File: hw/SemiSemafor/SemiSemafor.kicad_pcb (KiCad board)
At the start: 2 copper layers, 40.2 x 63.1 mm, 44 parts, among them J1 USB_PCB, J2 ESP-Programing_conector, SW1 SW_DIP_x01, SW2 SW_DIP_x01, U1 LD39200, U2 ESP32-C3-MINI-1, U3 LIS2DH12

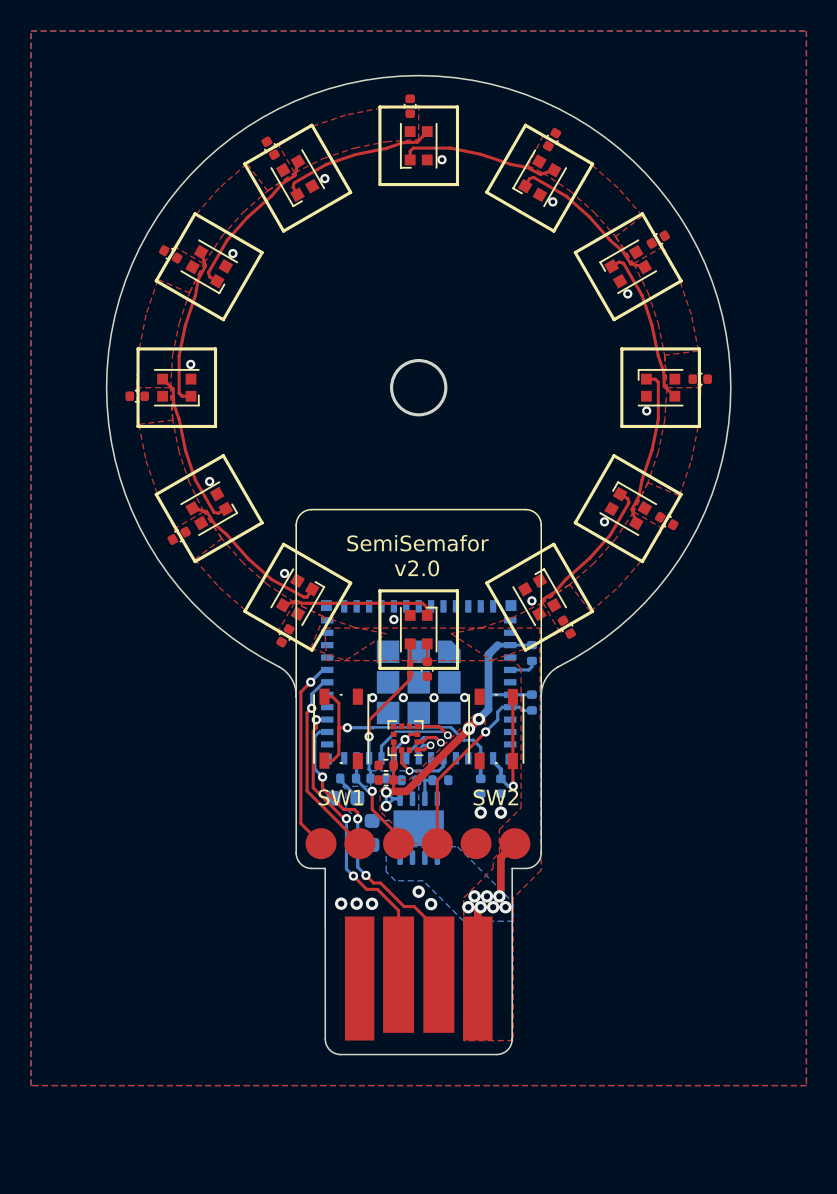
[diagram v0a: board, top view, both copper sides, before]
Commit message: 5mm LED
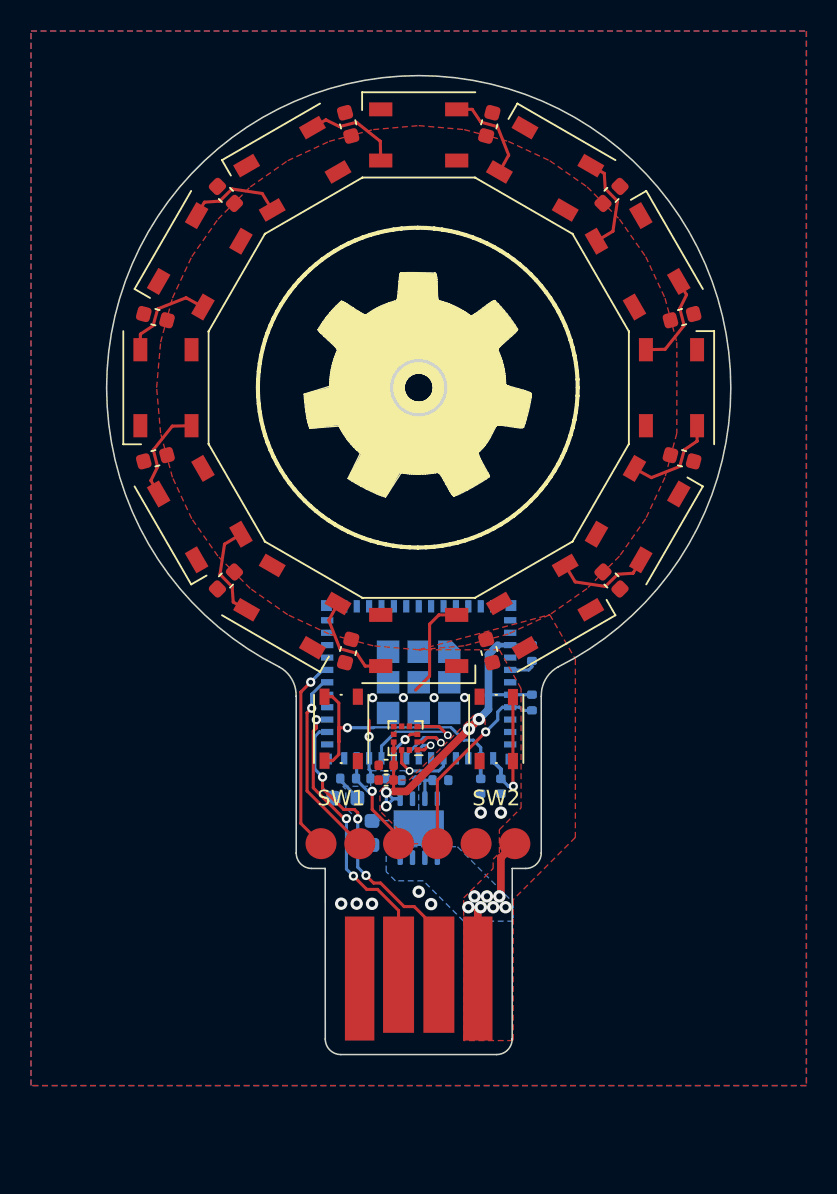
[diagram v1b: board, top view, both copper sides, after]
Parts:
- removed FB1: FerriteBead, Inductor_SMD:L_0201_0603Metric
- C1, C10, C11, C12, C13, C14, C15, C2, C3, C4, C5, C9: footprint Capacitor_SMD:C_0402_1005Metric -> Capacitor_SMD:C_0603_1608Metric
- D1, D10, D11, D12, D2, D3, D4, D5, D6, D7, D8, D9: footprint LED_SMD:LED_WS2812B-2020_PLCC4_2.0x2.0mm -> LED_SMD:LED_WS2812B_PLCC4_5.0x5.0mm_P3.2mm
- moved C11 5.23 mm to (162.4, 67.6), turned to 45 degrees
- moved C2 5.23 mm to (137.6, 92.4), turned to -135 degrees
- moved C14 5.23 mm to (162.4, 92.4), turned to -45 degrees
- moved C5 5.23 mm to (137.6, 67.6), turned to 135 degrees
- moved C12 5.23 mm to (167.0, 75.5), turned to 15 degrees
- moved C3 5.23 mm to (133.0, 84.5), turned to -165 degrees
- moved C9 5.23 mm to (145.5, 63.0), turned to 105 degrees
- moved C15 5.23 mm to (154.5, 97.0), turned to -75 degrees
- moved C1 5.23 mm to (145.4, 97.0), turned to -105 degrees
- moved C10 5.23 mm to (154.6, 63.0), turned to 75 degrees
- moved C13 5.23 mm to (167.0, 84.5), turned to -15 degrees
- moved C4 5.23 mm to (133.0, 75.5), turned to 165 degrees
- moved D11 0.70 mm to (164.1, 88.2), turned to 60 degrees
- moved D3 0.70 mm to (135.9, 88.2), turned to -60 degrees
- moved D5 0.70 mm to (135.9, 71.8), turned to -120 degrees
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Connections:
- D1 pad 1: Net-(D1-DOUT) -> +5V
- D1 pad 2: GND -> Net-(D1-DOUT)
- D1 pad 3: Net-(D1-DIN) -> GND
- D1 pad 4: +5V -> Net-(D1-DIN)
- D10 pad 1: Net-(D10-DOUT) -> +5V
- D10 pad 2: GND -> Net-(D10-DOUT)
- D10 pad 3: Net-(D10-DIN) -> GND
- D10 pad 4: +5V -> Net-(D10-DIN)
- D11 pad 1: Net-(D11-DOUT) -> +5V
- D11 pad 2: GND -> Net-(D11-DOUT)
- D11 pad 3: Net-(D10-DOUT) -> GND
- D11 pad 4: +5V -> Net-(D10-DOUT)
- D12 pad 1: unconnected-(D12-DOUT-Pad1) -> +5V
- D12 pad 2: GND -> (no net)
- D12 pad 3: Net-(D11-DOUT) -> GND
- D12 pad 4: +5V -> Net-(D11-DOUT)
- D2 pad 1: Net-(D2-DOUT) -> +5V
- D2 pad 2: GND -> Net-(D2-DOUT)
- D2 pad 3: Net-(D1-DOUT) -> GND
- D2 pad 4: +5V -> Net-(D1-DOUT)
- D3 pad 1: Net-(D3-DOUT) -> +5V
- D3 pad 2: GND -> Net-(D3-DOUT)
- D3 pad 3: Net-(D2-DOUT) -> GND
- D3 pad 4: +5V -> Net-(D2-DOUT)
- D4 pad 1: Net-(D4-DOUT) -> +5V
- D4 pad 2: GND -> Net-(D4-DOUT)
- D4 pad 3: Net-(D3-DOUT) -> GND
- D4 pad 4: +5V -> Net-(D3-DOUT)
- D5 pad 1: Net-(D5-DOUT) -> +5V
- D5 pad 2: GND -> Net-(D5-DOUT)
- D5 pad 3: Net-(D4-DOUT) -> GND
- D5 pad 4: +5V -> Net-(D4-DOUT)
- D6 pad 1: Net-(D6-DOUT) -> +5V
- D6 pad 2: GND -> Net-(D6-DOUT)
- D6 pad 3: Net-(D5-DOUT) -> GND
- D6 pad 4: +5V -> Net-(D5-DOUT)
- D7 pad 1: Net-(D7-DOUT) -> +5V
- D7 pad 2: GND -> Net-(D7-DOUT)
- D7 pad 3: Net-(D6-DOUT) -> GND
- D7 pad 4: +5V -> Net-(D6-DOUT)
- D8 pad 1: Net-(D8-DOUT) -> +5V
- D8 pad 2: GND -> Net-(D8-DOUT)
- D8 pad 3: Net-(D7-DOUT) -> GND
- D8 pad 4: +5V -> Net-(D7-DOUT)
- D9 pad 1: Net-(D10-DIN) -> +5V
- D9 pad 2: GND -> Net-(D10-DIN)
- D9 pad 3: Net-(D8-DOUT) -> GND
- D9 pad 4: +5V -> Net-(D8-DOUT)
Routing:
- net Net-(D1-DIN): track 1.31 -> 6.62 mm
- net /I-LED: track 7.86 -> 3.79 mm
- net Net-(D6-DOUT): track 10.3 -> 6.32 mm
- net Net-(D3-DOUT): track 10.3 -> 6.32 mm
- net Net-(D10-DIN): track 10.3 -> 6.32 mm
- net Net-(D8-DOUT): track 10.3 -> 6.32 mm
- net Net-(D11-DOUT): track 10.3 -> 6.32 mm
- net Net-(D5-DOUT): track 10.3 -> 6.32 mm
- net Net-(D4-DOUT): track 10.3 -> 6.32 mm
- net Net-(D10-DOUT): track 10.3 -> 6.32 mm
- net Net-(D7-DOUT): track 10.3 -> 6.32 mm
- net Net-(D2-DOUT): track 10.2 -> 6.32 mm
- net Net-(D1-DOUT): track 9.96 -> 6.32 mm
- net +5V: track 9.65 -> 8.58 mm
- net GND: vias 23 -> 11
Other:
- board text added: "Semafor-Accel v2.0"
- board text removed: "SemiSemafor v2.0"

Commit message: Ferit
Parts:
- added FB1: FerriteBead, Inductor_SMD:L_0201_0603Metric, F.Cu at (148.5, 100.0)
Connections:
- D12 pad 2: (no net) -> unconnected-(D12-DOUT-Pad2)
- U2 pad 7: +3.3V -> (no net)
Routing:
- net /I-LED: track 3.79 -> 6.03 mm
- net Net-(D1-DIN): track 6.62 -> 7.81 mm
- net GND: vias 11 -> 10
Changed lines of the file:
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@@
   (net 33 "Net-(D5-DOUT)")
   (net 34 "unconnected-(U3-INT2-Pad12)")
+  (net 35 "unconnected-(D12-DOUT-Pad2)")
   (footprint "LED_SMD:LED_WS2812B_PLCC4_5.0x5.0mm_P3.2mm" (layer "F.Cu")
     (at 135.883786 71.85 -120)
@@
       (net 1 "+5V") (pinfunction "VDD") (pintype "power_in"))
     (pad "2" smd rect (at -2.45 1.65 30) (size 1.5 0.9) (layers "F.Cu" "F.Paste" "F.Mask")
-      (pinfunction "DOUT") (pintype "output+no_connect"))
+      (net 35 "unconnected-(D12-DOUT-Pad2)") (pinfunction "DOUT") (pintype "output+no_connect"))
     (pad "3" smd rect (at 2.45 1.65 30) (size 1.5 0.9) (layers "F.Cu" "F.Paste" "F.Mask")
       (net 2 "GND") (pinfunction "VSS") (pintype "power_in"))
@@
     )
   )
+  (footprint "Inductor_SMD:L_0201_0603Metric" (layer "F.Cu")
+    (at 148.5 100)
+    (descr "Inductor SMD 0201 (0603 Metric), square (rectangular) end terminal, IPC_7351 nominal, (Body size source: https://www.vishay.com/docs/20052/crcw0201e3.pdf), generated with kicad-footprint-generator")
+    (tags "inductor")
+    (property "LCSC" "C160965")
+    (property "Sheetfile" "SemiSemafor.kicad_sch")
+    (property "Sheetname" "")
+    (property "ki_description" "Ferrite bead")
+    (property "ki_keywords" "L ferrite bead inductor filter")
+    (attr smd)
+    (fp_text reference "FB1" (at 0 -1.05) (layer "F.SilkS") hide
+        (effects (font (size 1 1) (thickness 0.15)))
+    )
+    (fp_text value "FerriteBead" (at 0 1.05) (layer "F.Fab") hide
+        (effects (font (size 1 1) (thickness 0.15)))
+    )
+    (fp_text user "${REFERENCE}" (at 0 -0.68) (layer "F.Fab") hide
+        (effects (font (size 0.25 0.25) (thickness 0.04)))
+    )
+    (fp_line (start -0.7 -0.35) (end 0.7 -0.35)
+      (stroke (width 0.05) (type solid)) (layer "F.CrtYd"))
+    (fp_line (start -0.7 0.35) (end -0.7 -0.35)
+      (stroke (width 0.05) (type solid)) (layer "F.CrtYd"))
+    (fp_line (start 0.7 -0.35) (end 0.7 0.35)
+      (stroke (width 0.05) (type solid)) (layer "F.CrtYd"))
+    (fp_line (start 0.7 0.35) (end -0.7 0.35)
+      (stroke (width 0.05) (type solid)) (layer "F.CrtYd"))
+    (fp_line (start -0.3 -0.15) (end 0.3 -0.15)
+      (stroke (width 0.1) (type solid)) (layer "F.Fab"))
+    (fp_line (start -0.3 0.15) (end -0.3 -0.15)
+      (stroke (width 0.1) (type solid)) (layer "F.Fab"))
+    (fp_line (start 0.3 -0.15) (end 0.3 0.15)
+      (stroke (width 0.1) (type solid)) (layer "F.Fab"))
+    (fp_line (start 0.3 0.15) (end -0.3 0.15)
+      (stroke (width 0.1) (type solid)) (layer "F.Fab"))
+    (pad "" smd roundrect (at -0.345 0) (size 0.318 0.36) (layers "F.Paste") (roundrect_rratio 0.25))
+    (pad "" smd roundrect (at 0.345 0) (size 0.318 0.36) (layers "F.Paste") (roundrect_rratio 0.25))
+    (pad "1" smd roundrect (at -0.32 0) (size 0.46 0.4) (layers "F.Cu" "F.Mask") (roundrect_rratio 0.25)
+      (net 11 "/I-LED") (pintype "passive"))
+    (pad "2" smd roundrect (at 0.32 0) (size 0.46 0.4) (layers "F.Cu" "F.Mask") (roundrect_rratio 0.25)
+      (net 15 "Net-(D1-DIN)") (pintype "passive"))
+    (model "${KICAD6_3DMODEL_DIR}/Inductor_SMD.3dshapes/L_0201_0603Metric.wrl"
+      (offset (xyz 0 0 0))
+      (scale (xyz 1 1 1))
+      (rotate (xyz 0 0 0))
+    )
+  )
   (footprint "Resistor_SMD:R_0402_1005Metric" (layer "B.Cu")
     (at 157.3 97.11 90)
@@
     (pad "6" smd rect (at -5.9 0 180) (size 0.8 0.4) (layers "B.Cu" "B.Paste" "B.Mask")
       (net 21 "unconnected-(U2-GPIO3{slash}ADC1_CH3-Pad6)") (pinfunction "GPIO3/ADC1_CH3") (pintype "bidirectional"))
-    (pad "7" smd rect (at -5.9 -0.8 180) (size 0.8 0.4) (layers "B.Cu" "B.Paste" "B.Mask")
-      (net 3 "+3.3V"))
+    (pad "7" smd rect (at -5.9 -0.8 180) (size 0.8 0.4) (layers "B.Cu" "B.Paste" "B.Mask"))
     (pad "8" smd rect (at -5.9 -1.6 180) (size 0.8 0.4) (layers "B.Cu" "B.Paste" "B.Mask")
       (net 4 "/EN") (pinfunction "EN/CHIP_PU") (pintype "input"))
@@
   (via (at 150 112.5) (size 0.8) (drill 0.4) (layers "F.Cu" "B.Cu") (free) (net 2))
   (via (at 147.03 99.99) (size 0.6) (drill 0.3) (layers "F.Cu" "B.Cu") (free) (net 2))
-  (via (at 149.01 99.99) (size 0.6) (drill 0.3) (layers "F.Cu" "B.Cu") (free) (net 2))
   (via (at 145 113.27) (size 0.8) (drill 0.4) (layers "F.Cu" "B.Cu") (free) (net 2))
   (via (at 146 113.27) (size 0.8) (drill 0.4) (layers "F.Cu" "B.Cu") (free) (net 2))
@@
   (segment (start 146.55 97.95) (end 146 97.13) (width 0.2) (layer "F.Cu") (net 10))
   (segment (start 147.55 97.95) (end 146.55 97.95) (width 0.2) (layer "F.Cu") (net 10))
-  (segment (start 146.8 102.5) (end 146.8 101.450466) (width 0.2) (layer "F.Cu") (net 11))
+  (segment (start 146.8 102.5) (end 146.8 101) (width 0.2) (layer "F.Cu") (net 11))
+  (segment (start 147.8 100) (end 148.18 100) (width 0.2) (layer "F.Cu") (net 11))
+  (segment (start 146.8 101) (end 147.8 100) (width 0.2) (layer "F.Cu") (net 11))
   (via (at 146.8 102.5) (size 0.6) (drill 0.3) (layers "F.Cu" "B.Cu") (net 11))
   (segment (start 146.8 102.5) (end 146.8 103.9) (width 0.2) (layer "B.Cu") (net 11))
@@
   (segment (start 143.87 99) (end 144.1 99) (width 0.2) (layer "B.Cu") (net 14))
   (segment (start 150.7 95.25) (end 151.3 94.65) (width 0.2) (layer "F.Cu") (net 15))
-  (segment (start 151.3 94.65) (end 152.45 94.65) (width 0.2) (layer "F.Cu") (net 15))
-  (segment (start 149.8 99.5) (end 150.7 98.6) (width 0.2) (layer "F.Cu") (net 15))
+  (segment (start 148.82 100) (end 149.3 100) (width 0.2) (layer "F.Cu") (net 15))
   (segment (start 150.7 98.6) (end 150.7 95.25) (width 0.2) (layer "F.Cu") (net 15))
+  (segment (start 151.3 94.65) (end 152.45 94.65) (width 0.2) (layer "F.Cu") (net 15))
+  (segment (start 149.3 100) (end 150.7 98.6) (width 0.2) (layer "F.Cu") (net 15))
   (segment (start 137.185591 92.035208) (end 137.477053 90.090382) (width 0.2) (layer "F.Cu") (net 16))
   (segment (start 138.037212 93.820156) (end 137.970898 92.835015) (width 0.2) (layer "F.Cu") (net 16))

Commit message: moving the LED circle up
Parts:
- moved J1 3.00 mm to (150.0, 126.0)
- moved J2 3.00 mm to (156.2, 112.4)
- moved SW1 3.00 mm to (155.0, 105.0)
- moved SW2 3.00 mm to (145.0, 105.0)
- moved C18 1.66 mm to (147.9, 107.0)
- moved C17 1.62 mm to (147.9, 106.0)
- moved C16 1.51 mm to (147.0, 110.2)
- moved C6 1.51 mm to (145.3, 108.0)
- moved R4 1.51 mm to (157.3, 98.6)
- moved R5 1.51 mm to (157.3, 101.8)
- moved U2 1.51 mm to (150.0, 100.5)
- moved U3 1.51 mm to (149.2, 104.1)
- moved C7 1.51 mm to (154.0, 107.2)
- moved C8 1.51 mm to (155.3, 107.2)
- moved R10 1.51 mm to (151.4, 106.8)
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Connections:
- U2 pad 7: (no net) -> +3.3V
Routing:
- net /USB-D+: track 20.0 -> 24.0 mm, vias 3 -> 1
- net +3.3V: track 26.6 -> 29.8 mm
- net /USB-D-: track 20.6 -> 23.1 mm, vias 3 -> 1
- net /I-LED: track 6.03 -> 7.81 mm
- net /TX0: track 12.6 -> 14.2 mm
- net /EN: track 12.5 -> 14.0 mm
- net /BOOT: track 7.17 -> 8.60 mm
- net /RX0: track 12.5 -> 13.8 mm
- net /SW1: track 18.1 -> 16.9 mm
- net Net-(D1-DIN): track 7.81 -> 6.82 mm
- net GND: vias 10 -> 20
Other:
- board size 40.2 x 63.1 mm -> 40.2 x 66.1 mm

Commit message: v2.1.0
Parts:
- added G***: LOGO, LOGO, F.Cu at (150.0, 80.0)
- added J3: Conn_01x02, RKL-ESP:ESP-Small-programming connector, B.Cu at (150.0, 122.0)
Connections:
- U2 pad 7: +3.3V -> (no net)
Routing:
- net /EN: track 14.0 -> 24.0 mm, vias 1 -> 2
- net /BOOT: track 8.60 -> 18.3 mm, vias 1 -> 2
- net GND: vias 20 -> 22
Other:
- outline, holes or cut-outs redrawn
- board text added: "EN B"
- board text added: "Semafor-Accel v2.1.0 vzorek.com/semafor"
- board text added: "T R B EN G 5"
- board text removed: "Semafor-Accel v2.0"
